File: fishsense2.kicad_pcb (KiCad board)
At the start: 2 copper layers, 86.4 x 49.5 mm, 26 parts, among them J1 Conn_02x10_Odd_Even, J11 Screw_Terminal_01x02, J2 BATT_OUT, J3 BATT_IN, Q1 Q_NMOS_GSD, Q2 Q_PMOS_GDS, SW1 SW_Reed, SW2 SW_SPST, U1 R3119, U5 P783F-Q24-S5-S

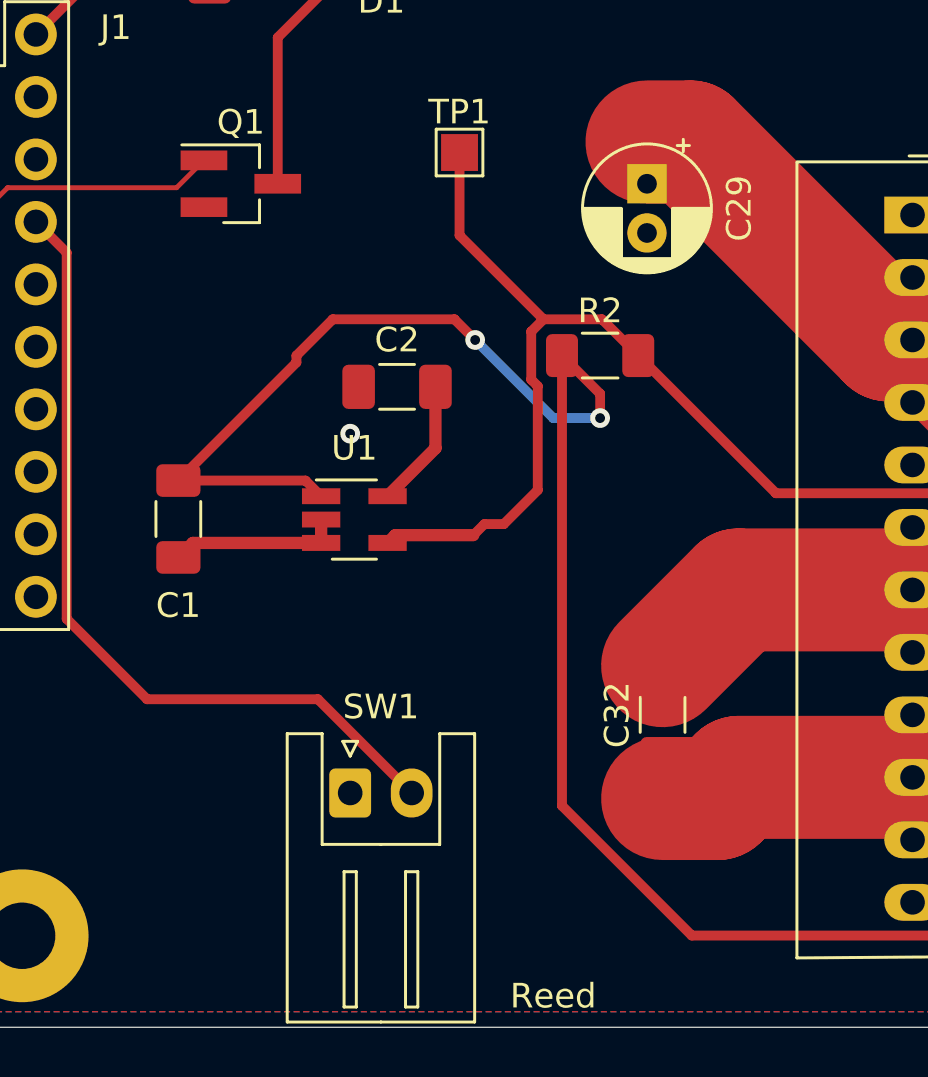
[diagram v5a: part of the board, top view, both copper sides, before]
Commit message: Swapped tps3711 for tl7702b because of availability. Added extra hysteresis to voltage supervisor.
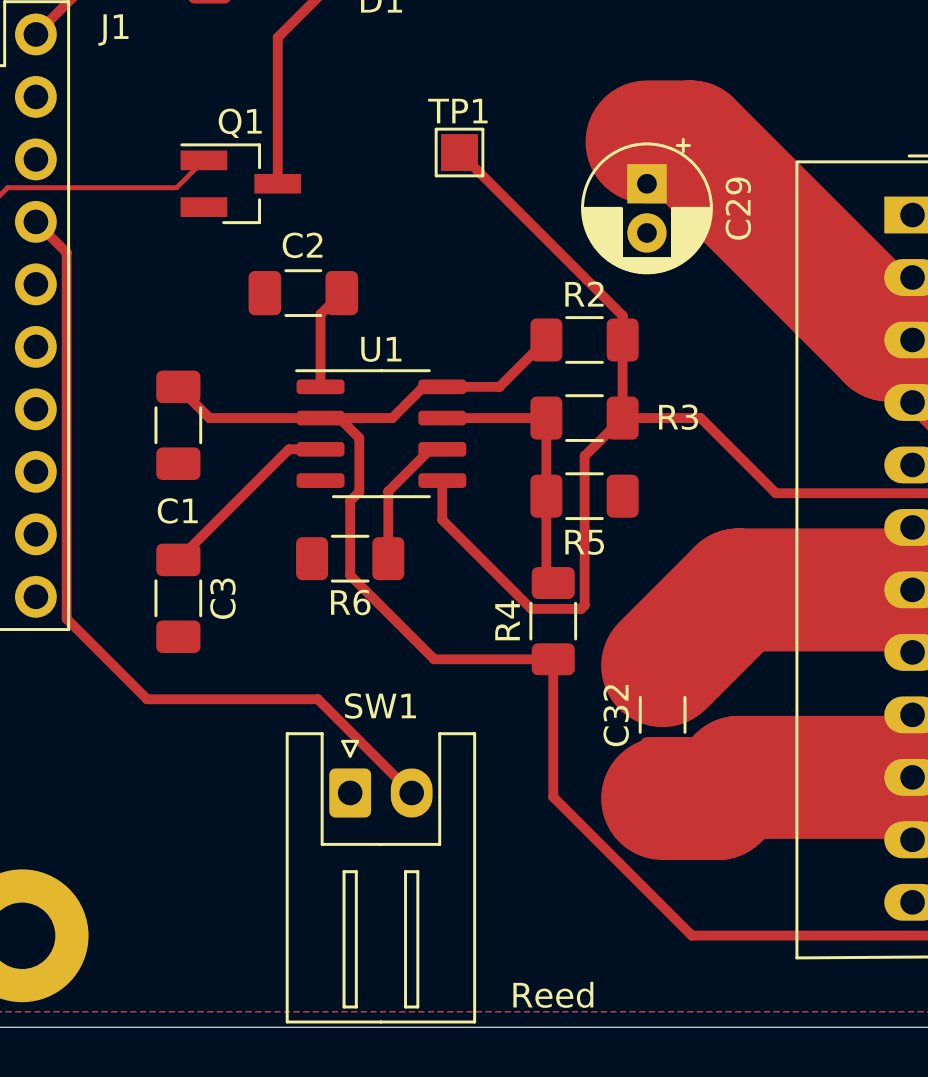
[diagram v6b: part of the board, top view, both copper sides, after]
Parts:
- added C3: 100n, Capacitor_SMD:C_1206_3216Metric_Pad1.33x1.80mm_HandSolder, F.Cu at (127.0, 143.9)
- added R3: 1M, Resistor_SMD:R_1206_3216Metric_Pad1.30x1.75mm_HandSolder, F.Cu at (143.5, 136.5)
- added R4: 34.8k, Resistor_SMD:R_1206_3216Metric_Pad1.30x1.75mm_HandSolder, F.Cu at (142.2, 144.8)
- added R5: 102k, Resistor_SMD:R_1206_3216Metric_Pad1.30x1.75mm_HandSolder, F.Cu at (143.5, 139.7)
- added R6: 50k, Resistor_SMD:R_1206_3216Metric_Pad1.30x1.75mm_HandSolder, F.Cu at (134.0, 142.2)
- C2: value 10n -> 100n
- R2: value 100k -> 50k
- U1: value R3119 -> TL7702A; footprint Package_TO_SOT_SMD:SOT-23-5_HandSoldering -> Package_SO:SOIC-8_3.9x4.9mm_P1.27mm
- moved C2 5.39 mm to (132.1, 131.4)
- moved C1 3.81 mm to (127.0, 136.8)
- moved U1 3.66 mm to (135.3, 137.2)
- moved R2 0.90 mm to (143.5, 133.3)
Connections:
- U1 pad 1: +12V -> Net-(C2-Pad1)
- U1 pad 2: GND -> +12V
- U1 pad 3: GND -> Net-(C3-Pad1)
- U1 pad 4: /Power/POWEROFF_OD -> GND
- U1 pad 5: Net-(C2-Pad1) -> /Power/POWEROFF_OD
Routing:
- net Net-(R3-Pad2): track 0.00 -> 11.1 mm
- net +12V: track 92.0 -> 82.9 mm, vias 2 -> 0
- net Net-(C3-Pad1): track 0.00 -> 7.64 mm
- net GND: track 18.4 -> 11.4 mm, vias 1 -> 0
- net Net-(R6-Pad1): track 0.00 -> 5.64 mm
- net /Power/POWEROFF_OD: track 66.0 -> 69.4 mm
- net Net-(C2-Pad1): track 5.25 -> 4.17 mm

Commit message: Many changes from first design review.
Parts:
- removed J11: Screw_Terminal_01x02, TerminalBlock:TerminalBlock_bornier-2_P5.08mm
- removed SW1: SW_Reed, Connector_JST:JST_XH_S2B-XH-A_1x02_P2.50mm_Horizontal
- added J4: V_ORBITTY, Connector_JST:JST_XH_S2B-XH-A_1x02_P2.50mm_Horizontal, F.Cu at (193.7, 128.9)
- added J5: V_HUB, Connector_JST:JST_XH_S2B-XH-A_1x02_P2.50mm_Horizontal, F.Cu at (193.7, 142.9)
- added R10: 500k, Resistor_SMD:R_1206_3216Metric_Pad1.30x1.75mm_HandSolder, F.Cu at (146.1, 150.5)
- added R7: 130, Resistor_SMD:R_1206_3216Metric_Pad1.30x1.75mm_HandSolder, F.Cu at (130.8, 120.7)
- added R8: 130, Resistor_SMD:R_1206_3216Metric_Pad1.30x1.75mm_HandSolder, F.Cu at (126.4, 125.7)
- added RV1: 1M, Potentiometer_SMD:Potentiometer_Bourns_3269W_Vertical, F.Cu at (137.8, 153.0)
- added TP2: GND, TestPoint:TestPoint_Plated_Hole_D2.0mm, F.Cu at (137.2, 113.7)
- added TP3: 12v, TestPoint:TestPoint_Plated_Hole_D2.0mm, F.Cu at (151.8, 113.7)
- added TP4: GPIO, TestPoint:TestPoint_Plated_Hole_D2.0mm, F.Cu at (142.9, 113.7)
- D1: value LED -> RECORD_LED
- D4: value LED -> PWR_LED
- J1: value Conn_02x10_Odd_Even -> ORBITTY_EXPANSION; footprint Connector_PinHeader_2.54mm:PinHeader_2x10_P2.54mm_Vertical -> Connector_PinSocket_2.54mm:PinSocket_2x10_P2.54mm_Vertical
- J2: value BATT_OUT -> REED_SW; footprint TerminalBlock:TerminalBlock_bornier-2_P5.08mm -> Connector_JST:JST_XH_S2B-XH-A_1x02_P2.50mm_Horizontal
- J3: value BATT_IN -> EXT_PWR
- J6: renamed from SW2; value SW_SPST -> PWR_SWITCH
- R1: value 220 -> 130
- R9: value 220 -> 500k
- TP1, TP9: footprint TestPoint:TestPoint_Pad_1.5x1.5mm -> TestPoint:TestPoint_Plated_Hole_D2.0mm
- moved J2 76.2 mm to (127.6, 151.1), turned to 0 degrees
- moved TP9 53.9 mm to (156.2, 113.7)
- moved R9 42.0 mm to (146.1, 155.6), turned to 0 degrees
- moved C32 25.4 mm to (171.4, 154.3), turned to 270 degrees
- moved TP1 15.0 mm to (147.3, 113.7)
- moved F1 11.4 mm to (179.1, 155.6)
- moved Q2 7.24 mm to (187.3, 142.9)
- moved Q1 5.12 mm to (134.6, 126.4)
- moved D1 4.44 mm to (132.1, 115.6)
- moved J1 2.68 mm to (121.3, 120.9)
- moved J6 0.64 mm to (165.7, 121.3)
- moved J3 0.63 mm to (180.3, 125.1)
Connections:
- net RELAY_CTL renamed Net-(J1-Pad10)
- C1 pad 1: +12V -> /Power/Vext
- C29 pad 1: /Power/BATT_SWITCHED -> +12V
- F1 pad 1: +12V -> /Power/Vext
- J1 pad 9: REED -> Net-(J1-Pad9)
- J2 pad 1: GND -> Net-(J1-Pad8)
- J2 pad 2: /Power/BATT_SWITCHED -> GND
- Q1 pad 1: Net-(J1-Pad7) -> Net-(Q1-Pad1)
- Q2 pad 2: /Power/BATT_SWITCHED -> +12V
- Q2 pad 3: +12V -> /Power/Vext
- R2 pad 1: +12V -> /Power/Vext
- R4 pad 1: +12V -> /Power/Vext
- R9 pad 1: Net-(J1-Pad2) -> +5V
- R9 pad 2: Net-(D1-Pad2) -> Net-(R10-Pad1)
- U1 pad 2: +12V -> /Power/Vext
- U1 pad 8: +12V -> /Power/Vext
- U5 pad 12: Net-(U5-Pad12) -> Net-(R10-Pad1)
- U5 pad 2: /Power/BATT_SWITCHED -> +12V
- U5 pad 3: /Power/BATT_SWITCHED -> +12V
- U5 pad 4: /Power/BATT_SWITCHED -> +12V
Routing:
- net /Power/Vext: track 0.00 -> 88.0 mm, vias 0 -> 1
- net /Power/BATT_SWITCHED: track 78.0 -> 0.00 mm
- net +5V: track 96.7 -> 164.1 mm, vias 1 -> 3
- net Net-(J1-Pad9): track 0.00 -> 33.4 mm
- net Net-(R10-Pad1): track 0.00 -> 25.7 mm
- net /Power/POWEROFF_OD: track 69.4 -> 89.5 mm, vias 0 -> 1
- net GND: track 11.4 -> 0.00 mm, vias 0 -> 8
- net Net-(F1-Pad2): track 14.5 -> 23.1 mm
- net Net-(J1-Pad2): track 7.85 -> 0.00 mm
- net Net-(J1-Pad8): track 33.6 -> 26.7 mm
- net Net-(J1-Pad7): track 10.4 -> 4.63 mm
- net Net-(Q1-Pad1): track 0.00 -> 5.34 mm
- net +12V: track 82.9 -> 81.1 mm
- net Net-(J3-Pad2): track 11.2 -> 9.61 mm
- net Net-(D1-Pad2): track 5.86 -> 5.20 mm
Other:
- board text added: "Fishsense PIO Rev. 2 SN"
- board text removed: "12v Out"
- board text removed: "5V Out"
- board text removed: "Battery In"
- board text removed: "PWR"
- board text removed: "Power Switch"
- board text removed: "Record"
- board text removed: "Reed"

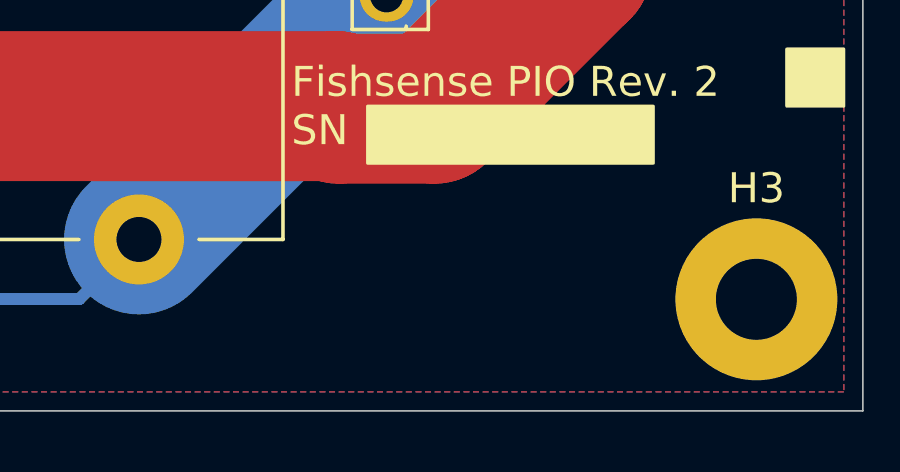
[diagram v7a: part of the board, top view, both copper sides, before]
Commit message: Added logo to PCB. Changed resistance to preferred value.
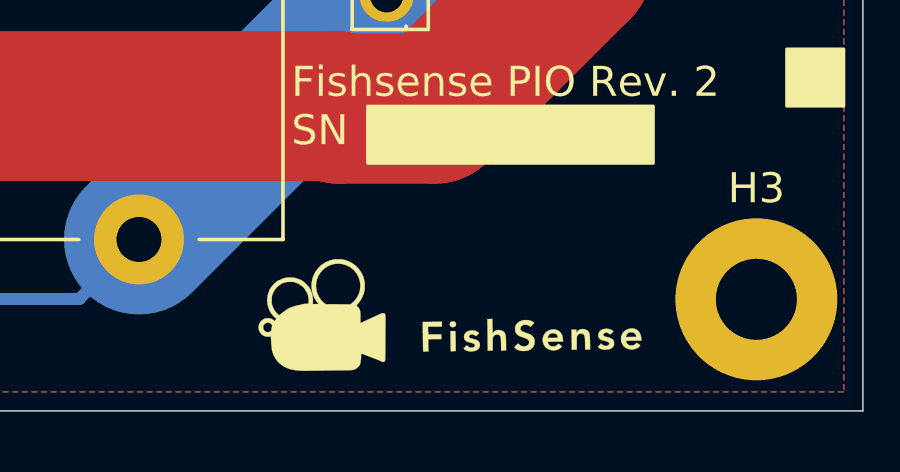
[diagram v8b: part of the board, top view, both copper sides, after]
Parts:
- added G***: LOGO, fishsense2:logo, F.Cu at (189.2, 158.8)
